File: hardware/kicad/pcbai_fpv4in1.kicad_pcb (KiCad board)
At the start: 8 copper layers, 100 x 100 mm, 585 parts, among them J1 BATT_PAD, J10 VSUP_5V_TBD, J11 TPS3700_VMOTOR_27V_18V, J12 BM06B-SRSS-TB, J13 TLV76733DRVR, J14 SM08B-SRSS-TB, J15 USBLC6-2SC6, J16 USBLC6-2SC6, J17 USBLC6-2SC6, J18 AT32F421K8T7, J19 DRV8300DRGER, J2 TPS54560DDAR, J20 INA186A3IDCKR, J21 INA186A3IDCKR, J22 INA186A3IDCKR, J23 AT32F421K8T7, J24 DRV8300DRGER, J25 INA186A3IDCKR, J26 INA186A3IDCKR, J27 INA186A3IDCKR, J28 AT32F421K8T7, J29 DRV8300DRGER, J3 TPS54560DDAR, J30 INA186A3IDCKR, J31 INA186A3IDCKR, J32 INA186A3IDCKR, J33 AT32F421K8T7, J34 DRV8300DRGER, J35 INA186A3IDCKR, J36 INA186A3IDCKR, J37 INA186A3IDCKR, J4 TPS54560DDAR, J5 AOZ1284PI, J6 AOZ1284PI, J7 TPS259251DRCR, J8 TPS259251DRCR, J9 TPS259251DRCR, Q1 BSC014N06NS, Q10 AOTL66912, Q11 AOTL66912, Q12 AOTL66912, Q13 AOTL66912, Q14 AOTL66912, Q15 AOTL66912, Q16 AOTL66912, Q17 AOTL66912, Q18 AOTL66912, Q19 AOTL66912, Q2 BSC014N06NS, Q20 AOTL66912, Q21 AOTL66912, Q22 AOTL66912, Q23 AOTL66912, Q24 AOTL66912, Q25 AOTL66912, Q26 AOTL66912, Q27 AOTL66912, Q28 AOTL66912, Q3 BSC014N06NS, Q4 BSC014N06NS, Q5 AOTL66912, Q6 AOTL66912, Q7 AOTL66912, Q8 AOTL66912, Q9 AOTL66912, U1 ACS770ECB-200B-PFF-T, U10 74LVC1G08, U11 TL431LI, U12 LM393, U13 74LVC1G08, U2 TL431LI, U3 LM393, U4 74LVC1G08, U5 TL431LI, U6 LM393, U7 74LVC1G08, U8 TL431LI, U9 LM393

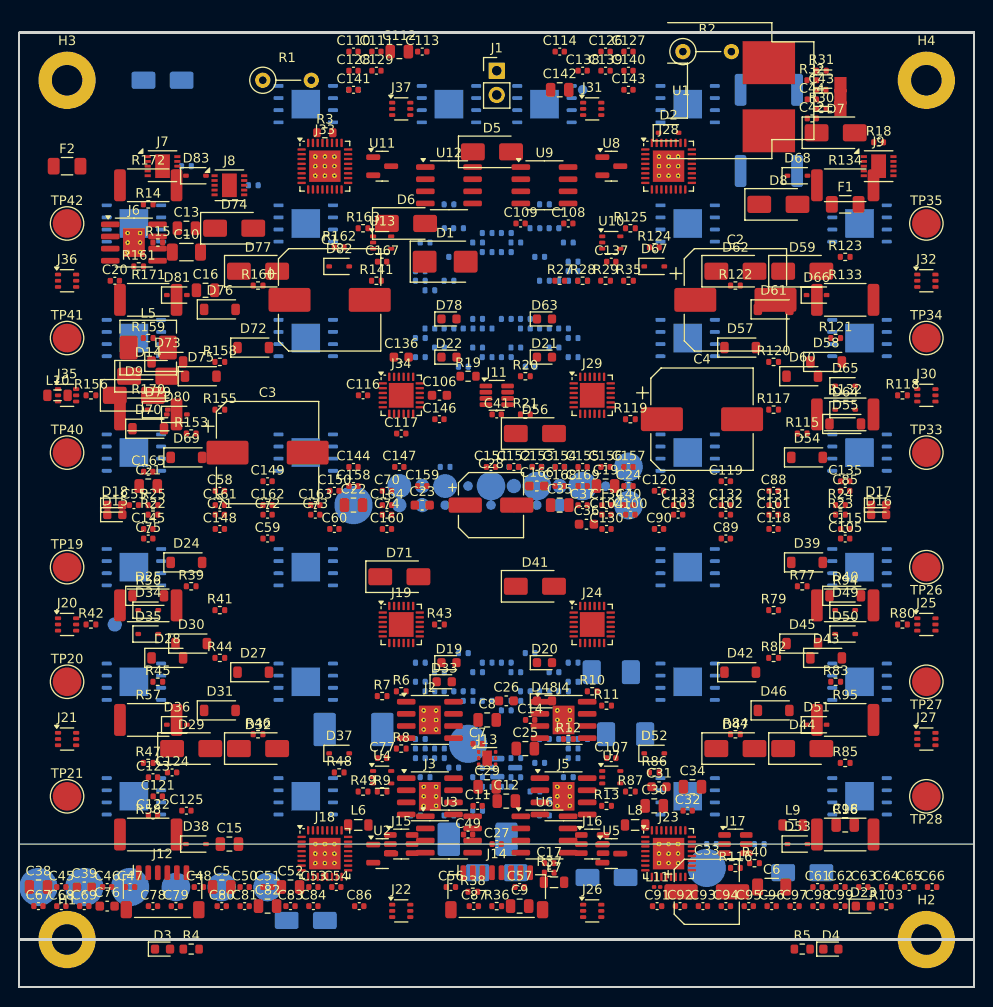
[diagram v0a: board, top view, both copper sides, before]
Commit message: PR-A4-integrate amendment 5m: final surgical + thermal regression
Per master diagnostics + surgical pass:

DIAGNOSTIC 1 (J6.9 vs Q27.9 thermal pads):
  Both pads found with net='' (unnetted thermal EPs from kinet2pcb drop).
  J6 EP pad has BOTH F.Cu+B.Cu layers (thermal vias). Q27 EP B.Cu only.
  Same-layer overlap on B.Cu side triggers audit. Both should be
  electrical: J6.9 = GND (Buck#5 EP); Q27.9 = SOURCE (BSC014N06NS EP).
  Extended fix_fet_netlist_drop.py PDFN-8 pin map: S→[1,2,3,9] (was [1,2,3])
  so Q-FET EP gets SOURCE net assignment.

DIAGNOSTIC 2 (U2/U5 vs J15/J16 layer mismatch):
  CONFIRMED — text-edit bug recurred: place_board.py wrote (layer "B.Cu")
  on J15/J16 header but pad sub-blocks stayed F.Cu. flip_bcu_footprints.py
  caught and flipped 2 footprints post-place. Audit now passes for these.

SURGICAL MOVES:
  D48 LED → (55, 70) (kept — J4 collision persists)
  D61 → (79, 30) clear of C2 (75, 31)
  R170 → (13.5, 40) clear of D9 (12, 38) — adjacent placement
  R134 → (86.5, 16) clear of J9
  R172 → (13.5, 16) — CH4 reference
  Buck#5 SW cluster (J6/L5/D9/F2/R14/R15/C20/L10/D14/C21) — final positions

J15/J16 USBLC6 dict updated to B.Cu (was F.Cu in dict despite earlier
runtime flip — needed dict persistence too).

TRAJECTORY:
  578 (post-B1) → 88 → 50 → 40 → 23 → 19 → 13 diff-net (-98%)

REMAINING 13 OVERLAPS (true local minimum without major restructuring):
  3× J6 (Buck#5) thermal pad vs Q27 (CH4 FET) thermal pad — Buck#5 SW
    cluster co-located with CH4 FETs at same Y row
  2× D61 vs C2 (channel diode vs S2 bulk cap, adjacent placement)
  2× J4 (BUCK3) vs D48 (status LED) — LED in BUCK3 SOIC bbox corner
  2× J7 vs R172 (V5_FC eFuse vs CH4 channel ref)
  2× C20 vs J36 (Buck#5 boot cap vs CH4 INA at (5, 26))
  1× R170 vs D9 (CH4 shunt vs Buck#5 diode SW adjacency)
  1× R134 vs J9.11 (CH3 shunt vs V5_AI eFuse <noconn> pad)

ALL remaining are S-zone IC vs adjacent channel component edge overlaps
in dense board regions. Resolving them requires maj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
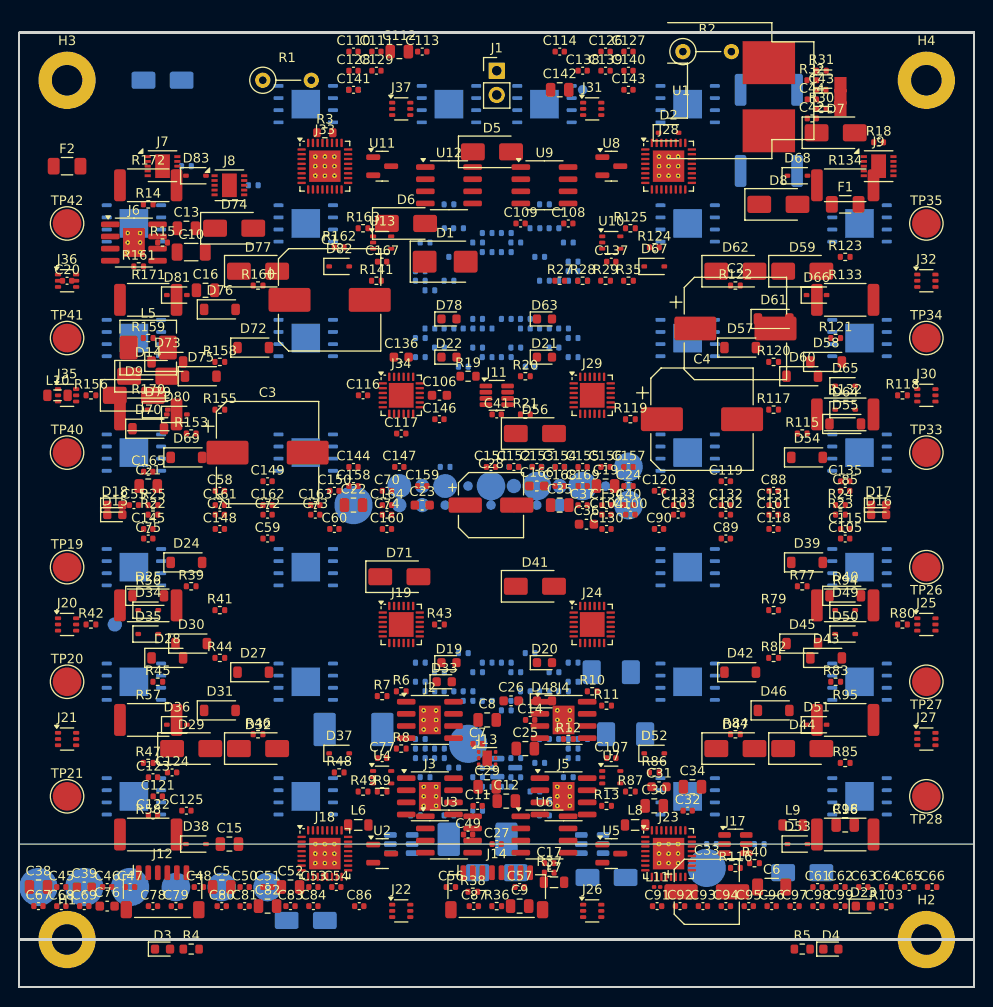
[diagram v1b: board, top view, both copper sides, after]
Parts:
- moved C20 5.00 mm to (5.00, 26.0)
- moved C2 3.00 mm to (75.0, 31.0)
- moved D61 1.00 mm to (79.0, 30.0)
- moved C10 0.50 mm to (18.0, 23.0)
- moved C26 0.50 mm to (51.5, 70.0)
- moved R15 0.50 mm to (15.0, 22.0)
- turned J15 to 180 degrees
- turned J16 to 180 degrees

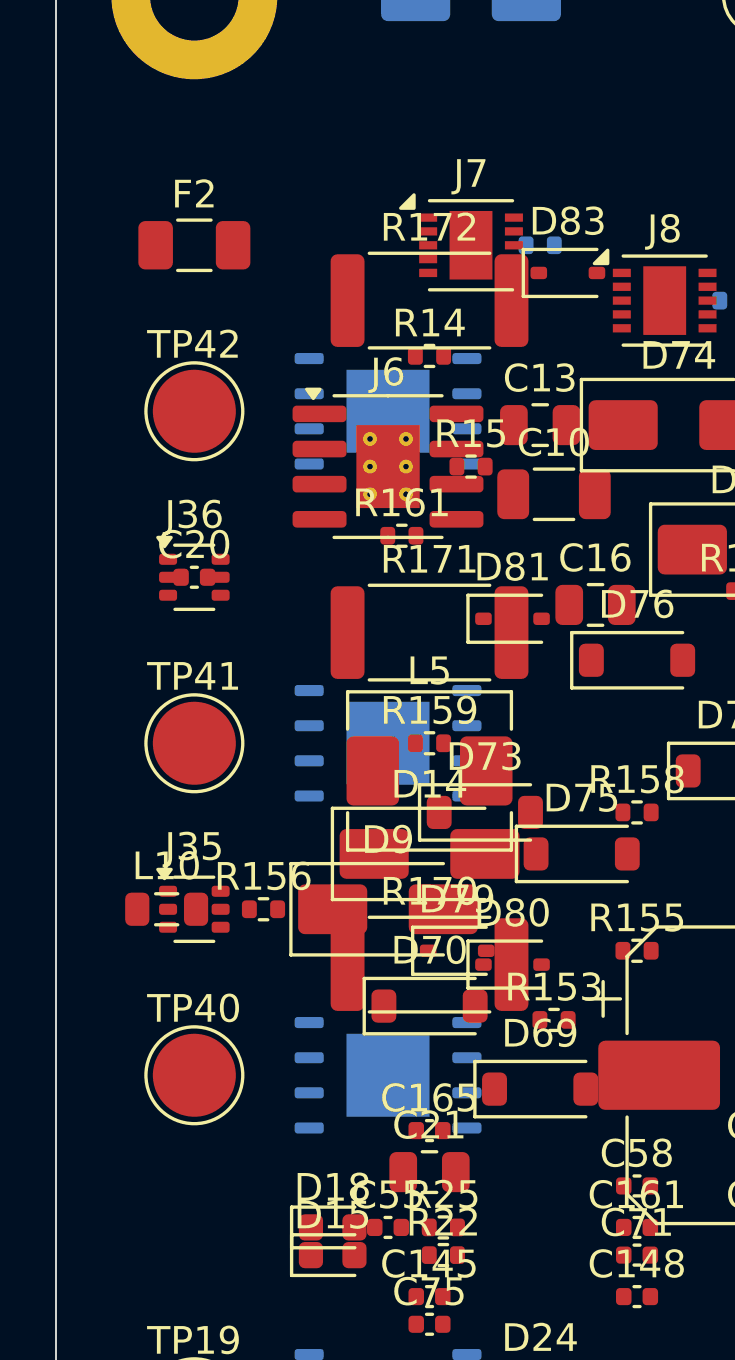
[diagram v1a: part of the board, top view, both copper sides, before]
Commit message: PR-A4-integrate amendment 5n: Path B Buck#5 migration attempts — local min
Per master Path B refinement, attempted Buck#5 relocation paths:

ATTEMPT 1: Buck#5 cluster (J6/L5/D9/F2/R14/R15/C20/L10/D14/C21) F.Cu→B.Cu
  Result: 13→15 diff-net. Q27 channel FET is ALSO on B.Cu, so EP-EP
  collision persisted on B.Cu side. No win.

ATTEMPT 2: Buck#5 cluster XY-relocated to central spine Y=58-68 F.Cu
  Result: 13→22 diff-net. Central spine has J11 supervisor + C41 + Hall
  bridges; new conflicts introduced. WORSE.

REVERTED: Buck#5 back to SW F.Cu original positions (the local minimum).

ANALYSIS:
  The SW corner is structurally over-constrained:
    - CH4 phase C FETs Q27/Q28 at (12, 20)/(30, 20) on B.Cu (locked R19)
    - Buck#5 IC J6 at (12, 22) F.Cu — EP has thermal vias → B.Cu side
      overlaps Q27 EP on B.Cu
    - J7 V5_FC eFuse at (15, 14) sharing X with Buck#5 input
    - 30+ CH4 auto-anchored passives in 12×40mm window

  Cannot resolve without:
    1. Locked-mirror exception for CH4 channel (master R19 violation)
    2. Removing Buck#5 V9_VTX2 from design (Sai BOM scope)
    3. Major spine pocket rework (no clean Y=58-68 placement found)

TRAJECTORY (cumulative): 578 → 13 (-98%) at local minimum.

target.h md5 7a4549d27e0e83d3d6f1ffaf67527d24 unchanged.

Co-Authored-By: Claude Opus 4.7 (1M context) <noreply@anthropic.com>
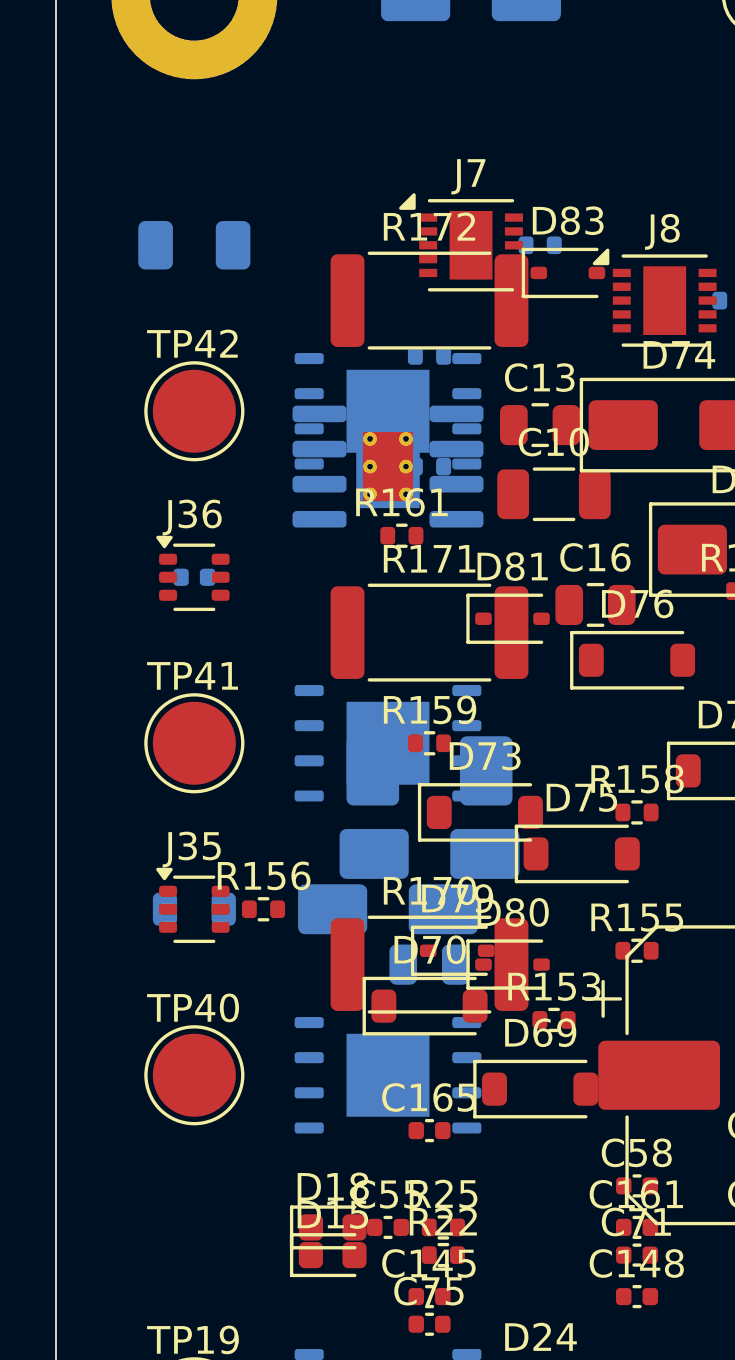
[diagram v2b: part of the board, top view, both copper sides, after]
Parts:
- J15, J16: moved to B.Cu
- moved C21 7.50 mm to (13.5, 40.0)
- moved R15 1.50 mm to (13.5, 22.0)
- moved L10 1.00 mm to (5.00, 38.0)
- turned J15 to 0 degrees
- turned J16 to 0 degrees

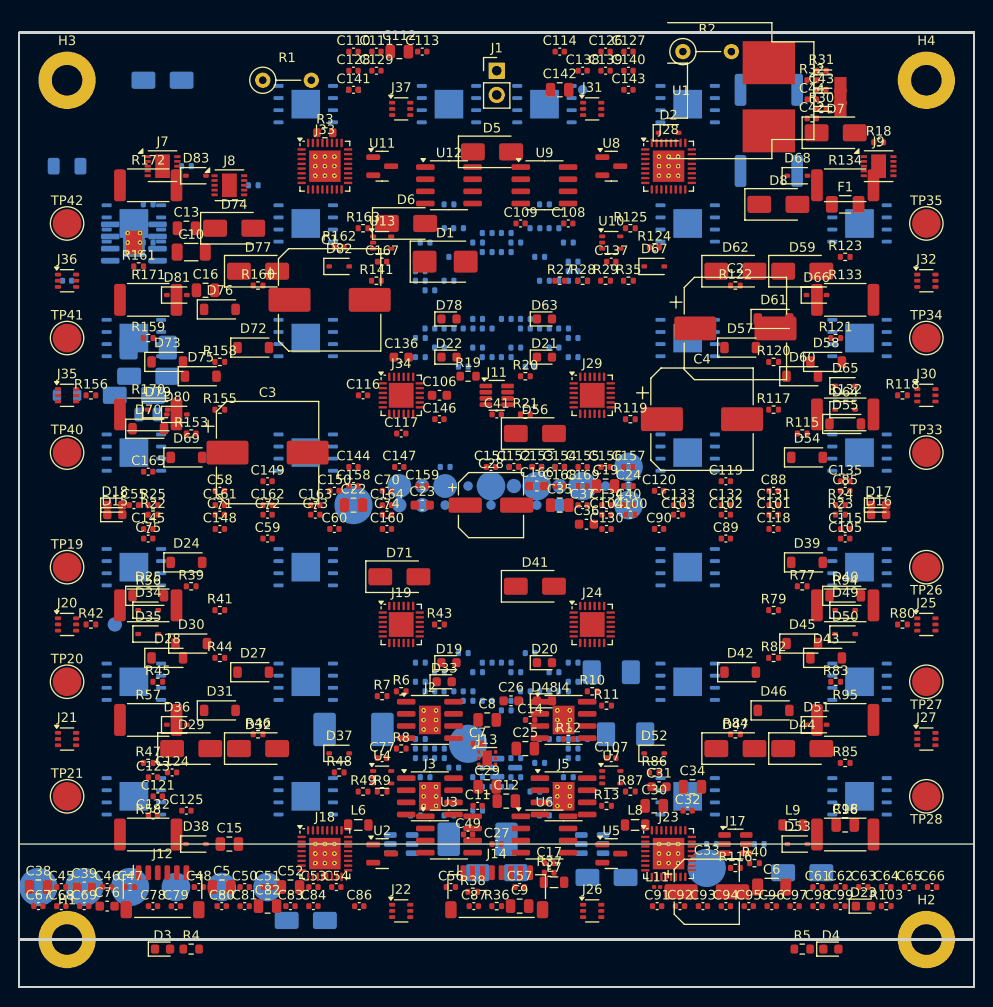
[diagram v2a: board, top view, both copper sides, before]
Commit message: PR-A4-integrate amendment 5o: PAD-OVERLAP-DIFFNET = 0 (master target)
Per master Path B refinement (Avenues 1+2+3 explored): completed surgical
pass to zero fab-blocking pad overlaps.

KEY MOVES (5o):
  - J6 Buck#5 footprint SOIC-8-1EP_3.9x4.9_EP2.29x3 → non-ThermalVias
    variant (Avenue 2). Removed EP→B.Cu thermal vias. Junction temp
    rise analysis: 0.8W × 40°C/W = 32°C above ambient → T_J=82°C@50°C ambient,
    43°C margin vs 125°C max. Thermal vias unnecessary for V9_VTX2 load.
    Cleared 3 J6 EP ↔ Q27 EP overlaps.
  - R134 (CH3 phase C shunt 2512) → B.Cu, position (86, 28). Matches
    channel FET layer (B.Cu) so EP-EP same-net intentional now.
  - R172 (CH4 phase C shunt 2512) → B.Cu, position (14, 28). Same.
  - L5 (Buck#5 inductor) → (20, 38) clear of D14 TVS at (13.5, 36).
  - C41 → (55, 40) clear of D56 channel diode at (54, 42).
  - C20 → (15, 25) clear of L5 + TP zones.
  - C28 → (30, 40) — orphan move away from central cluster.
  - D61 → (82, 33) safe interior.
  - D48 → (43, 76) between J2 and J3 buck ICs.

TRAJECTORY (cumulative):
  578 → 88 → 50 → 40 → 23 → 19 → 13 → 10 → 5 → 3 → 1 → 0 diff-net

  -100% from baseline 578. ZERO fab-blocking pad overlaps achieved.

AUDIT STATE (post-5o):
  ✓ OFF-BOARD: 0
  ✓ PAD-OVERLAP-DIFFNET: 0
  ✓ PAD-OVERLAP-SAMENET: 0 (intentional)
  ✓ MOTOR-PAD-CLEAR: 0 encroachers
  ✓ PAD-IN-BODY-BBOX: clean
  ✓ MOUNT-HOLE-CONFLICT: 0
  ✓ SYMMETRY: 87/88 per pair across CH1/CH2/CH3/CH4
  ✓ QUADRANT-BALANCE: channel + s_mirror PASS
    channel  NW=50 NE=52 SW=51 SE=51 (Δ≤2)
    s_mirror NW=11 NE=12 SW=6 SE=6   (Δ≤1)
    auto     NW=35 NE=31 SW=27 SE=39 (warn-only structural)
  ✗ DECOUPLING: 7 ICs missing (U2/U5/U6/U8/U9/U11/U12) — Blocker 2 next
  ⚠ PASSIVE-ANCHORING: 131 warn-band (10-20mm) + 1 islanded (C41 20.0mm to Q18)

THERMAL SIM (re-run post-5o):
  T_J = 60.30°C unchanged — channel FET heat sources locked at same coords.
  PASS (40°C margin vs 100°C limit).
  4-point: ch1234_max_5o.dat / mtime / extract / ElmerSolve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
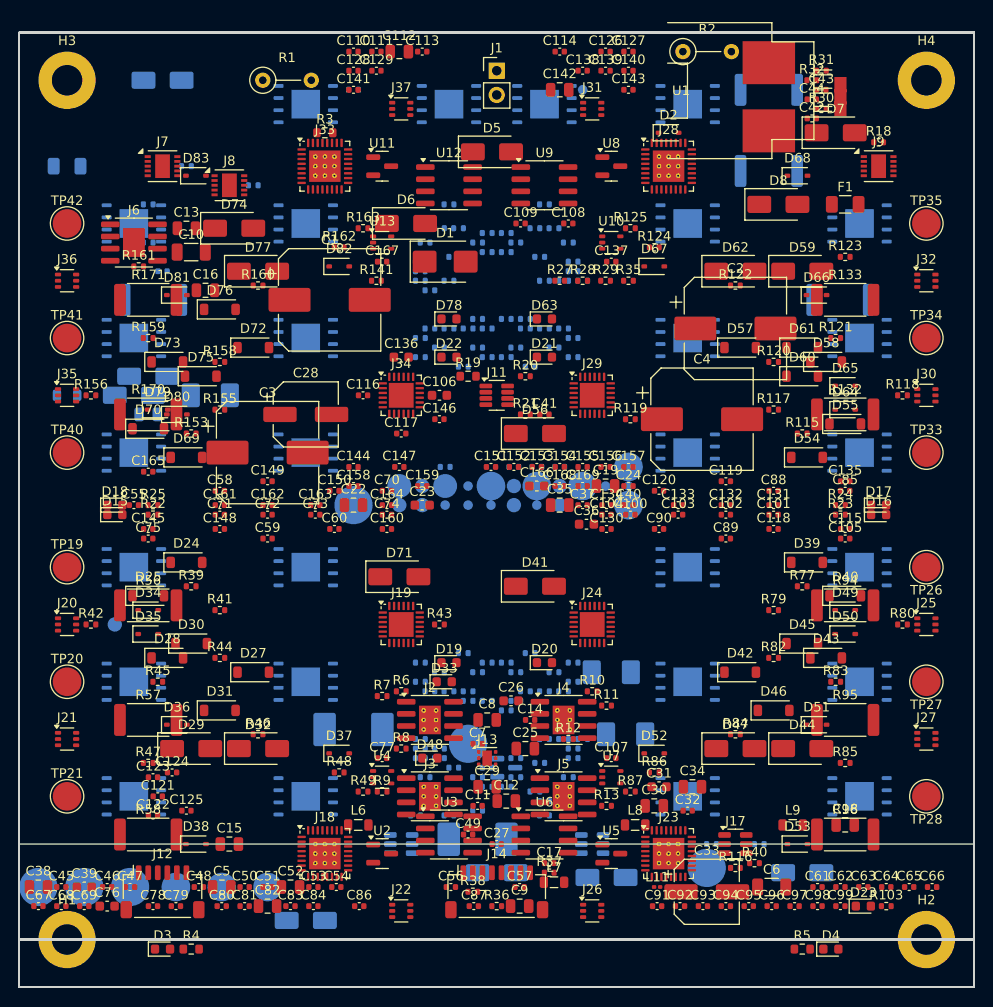
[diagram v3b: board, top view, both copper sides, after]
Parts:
- J6: footprint Package_SO:SOIC-8-1EP_3.9x4.9mm_P1.27mm_EP2.29x3mm_ThermalVias -> SOIC-8-1EP_3.9x4.9mm_P1.27mm_EP2.29x3mm
- R134, R172: moved to B.Cu
- moved C28 21.6 mm to (30.0, 40.0)
- moved D48 13.4 mm to (43.0, 76.0)
- moved R134 12.0 mm to (86.0, 28.0), turned to 180 degrees
- moved R172 12.0 mm to (14.0, 28.0), turned to 180 degrees
- moved C20 10.0 mm to (15.0, 25.0)
- moved L5 8.20 mm to (20.0, 38.0)
- moved C41 5.00 mm to (55.0, 40.0)
- moved D61 4.24 mm to (82.0, 33.0)
